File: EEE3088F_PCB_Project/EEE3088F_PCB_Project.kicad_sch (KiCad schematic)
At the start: 81 parts, among them IC1 DRV8833PWPR, IC2 DRV8833PWPR, IC3 TPS62067DSGR, IC5 INA219AIDCNR, IC7 TPS61088RHLR, J1 Conn_02x16_Odd_Even, J2 TYPE-C16PIN, J3 Conn_01x02, Q1 AO3400A, Q2 AO3400A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

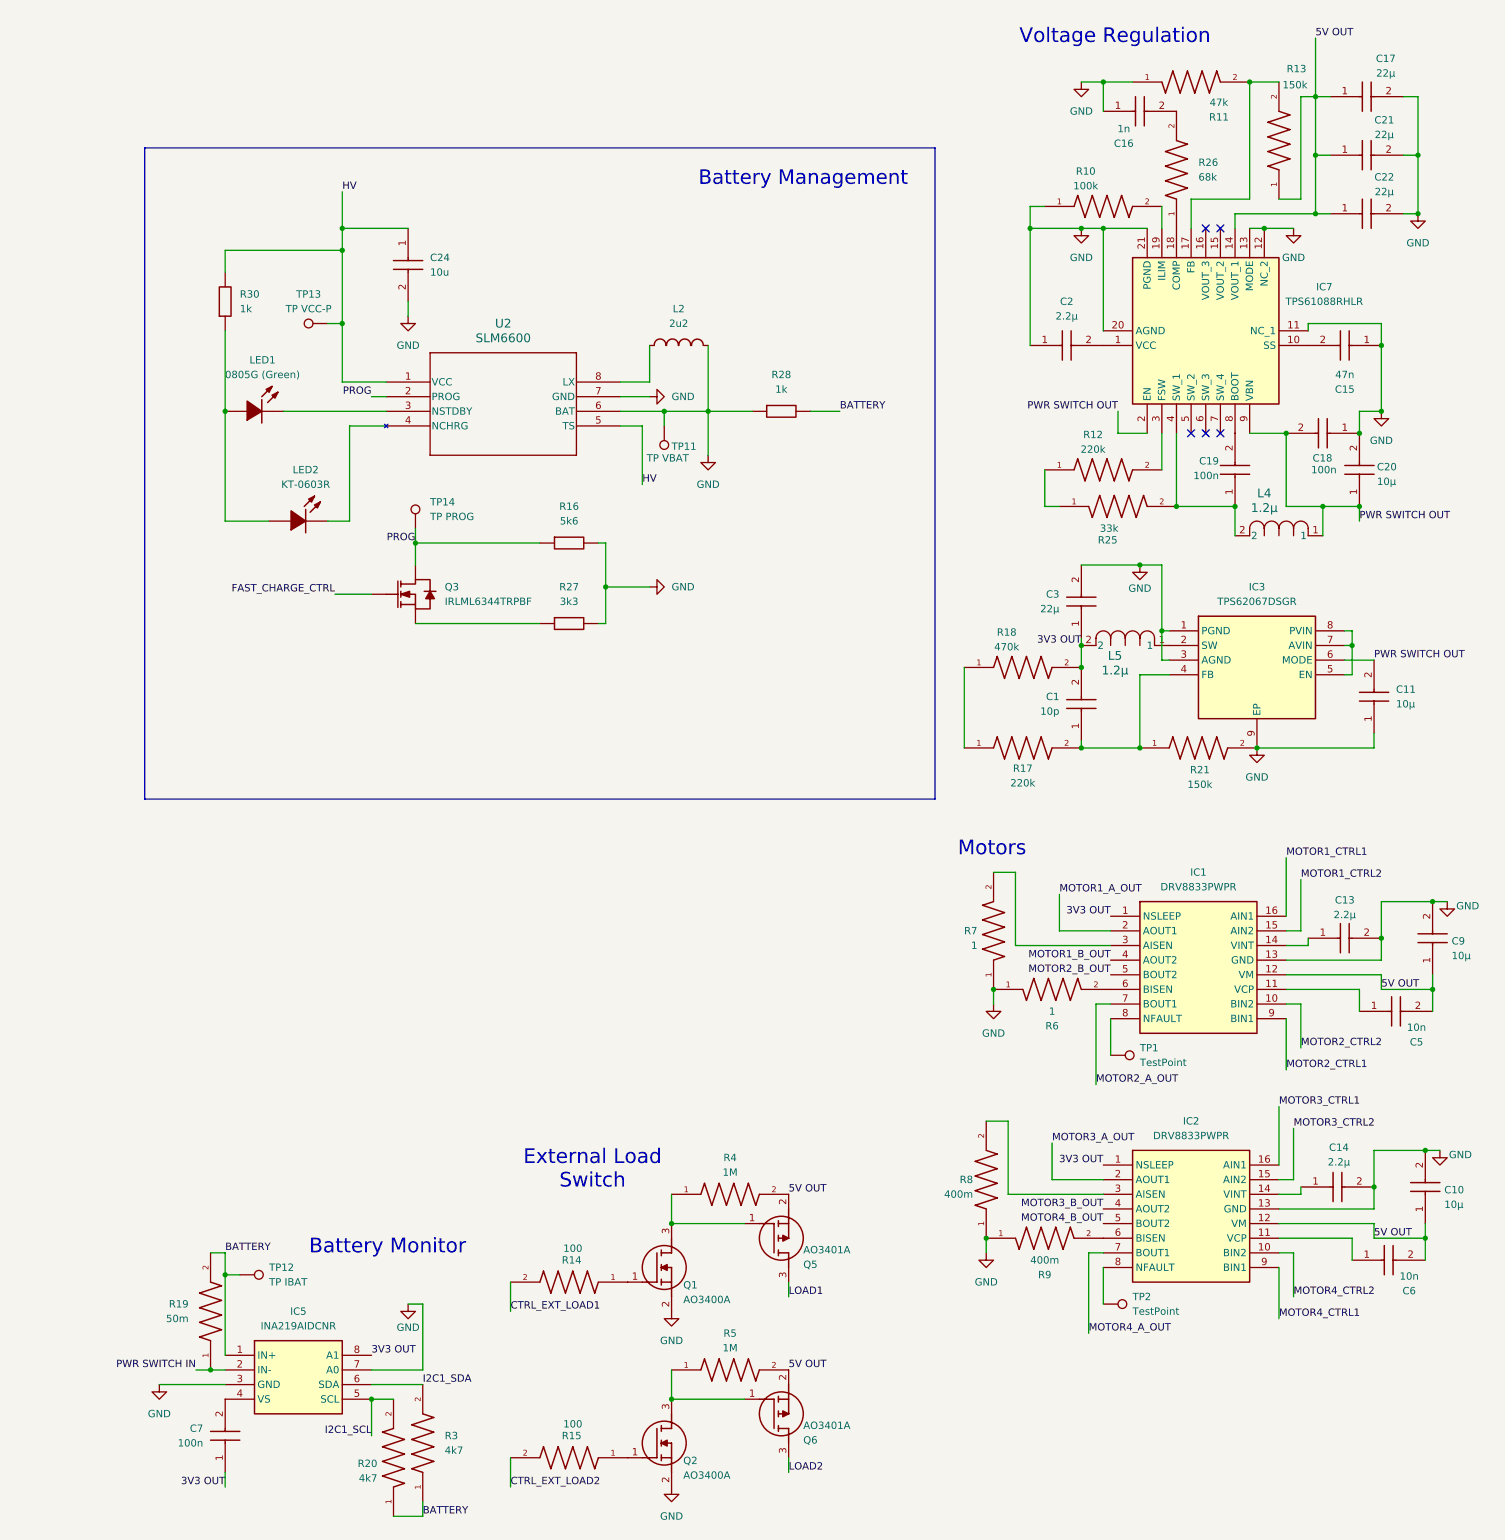
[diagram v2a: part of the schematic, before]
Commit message: V1.3.3
Added test points to my parts of the circuit
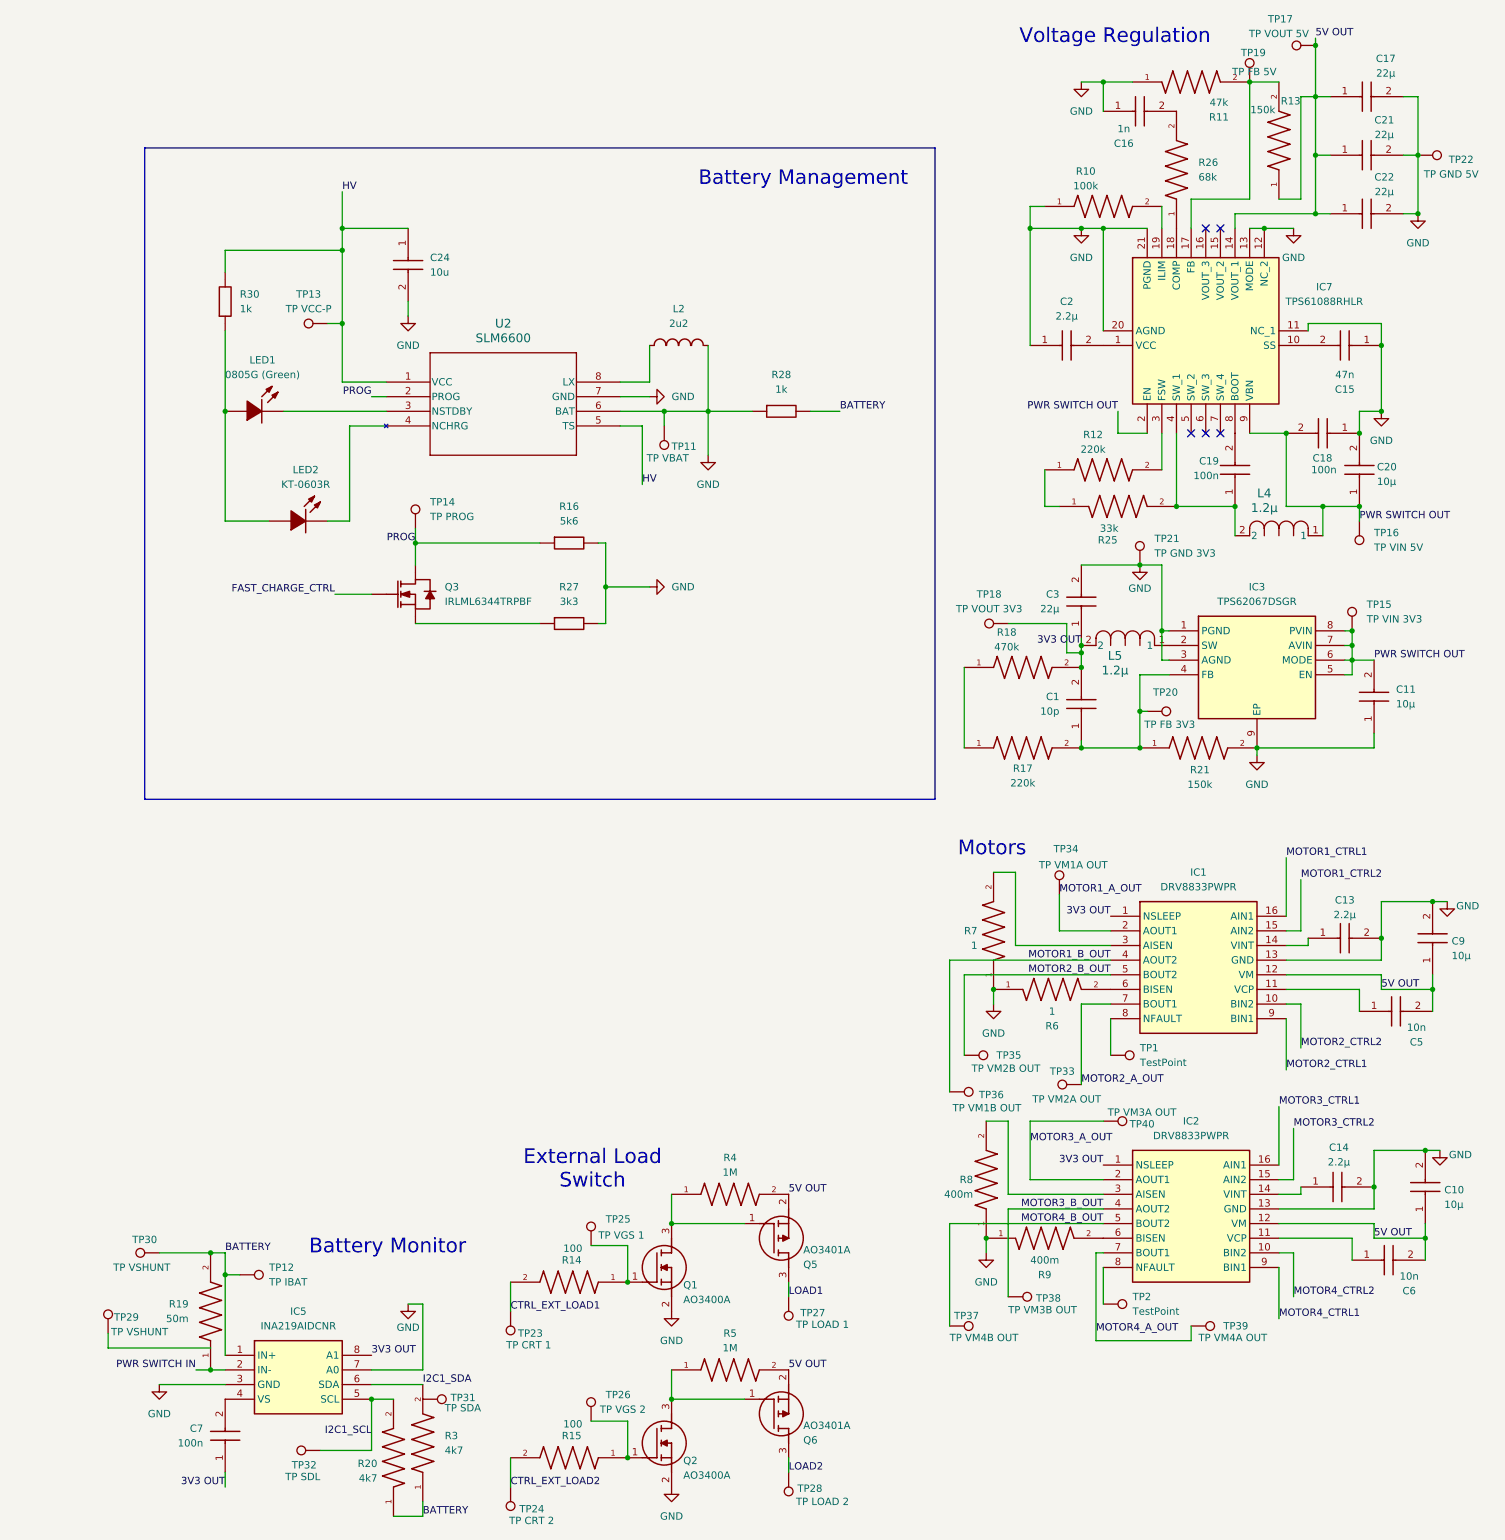
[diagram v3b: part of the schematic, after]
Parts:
- added TP15: TP VIN 3V3, symbol Connector:TestPoint
- added TP16: TP VIN 5V, symbol Connector:TestPoint
- added TP17: TP VOUT 5V, symbol Connector:TestPoint
- added TP18: TP VOUT 3V3, symbol Connector:TestPoint
- added TP19: TP FB 5V, symbol Connector:TestPoint
- added TP20: TP FB 3V3, symbol Connector:TestPoint
- added TP21: TP GND 3V3, symbol Connector:TestPoint
- added TP22: TP GND 5V, symbol Connector:TestPoint
- added TP23: TP CRT 1, symbol Connector:TestPoint
- added TP24: TP CRT 2, symbol Connector:TestPoint
- added TP25: TP VGS 1, symbol Connector:TestPoint
- added TP26: TP VGS 2, symbol Connector:TestPoint
- added TP27: TP LOAD 1, symbol Connector:TestPoint
- added TP28: TP LOAD 2, symbol Connector:TestPoint
- added TP29, TP30: TP VSHUNT, symbol Connector:TestPoint
- added TP31: TP SDA, symbol Connector:TestPoint
- added TP32: TP SDL, symbol Connector:TestPoint
- added TP33: TP VM2A OUT, symbol Connector:TestPoint
- added TP34: TP VM1A OUT, symbol Connector:TestPoint
- added TP35: TP VM2B OUT, symbol Connector:TestPoint
- added TP36: TP VM1B OUT, symbol Connector:TestPoint
- added TP37: TP VM4B OUT, symbol Connector:TestPoint
- added TP38: TP VM3B OUT, symbol Connector:TestPoint
- added TP39: TP VM4A OUT, symbol Connector:TestPoint
- added TP40: TP VM3A OUT, symbol Connector:TestPoint
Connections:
- net 3V3 OUT: now also TP18.1
- net 5V OUT: now also TP17.1
- net BATTERY: now also TP30.1
- net CTRL_EXT_LOAD1: now also TP23.1
- net CTRL_EXT_LOAD2: now also TP24.1
- net GND: now also TP21.1, TP22.1
- net I2C1_SCL: now also TP32.1
- net LOAD1: now also TP27.1
- net LOAD2: now also TP28.1
- net MOTOR1_A_OUT: now also TP34.1
- net MOTOR1_B_OUT: now also TP36.1
- net MOTOR2_A_OUT: now also TP33.1
- net MOTOR2_B_OUT: now also TP35.1
- net MOTOR3_A_OUT: now also TP40.1
- net MOTOR3_B_OUT: now also TP38.1
- net MOTOR4_A_OUT: now also TP39.1
- net MOTOR4_B_OUT: now also TP37.1
- net PWR SWITCH OUT: now also IC3.5 (EN), IC3.7 (AVIN), IC3.8 (PVIN), TP15.1, TP16.1
- net at Q2.1 (G), R15.1: now also TP26.1
- net at IC7.17 (FB), R11.2, R13.2: now also TP19.1
- net at C1.1, IC3.4 (FB), R17.2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: now also TP20.1
- net at Q1.1 (G), R14.1: now also TP25.1

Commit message: Revert "V1.3.3"
This reverts commit 82317ec0dd0d0933929f69b93ecb048d09c96738.
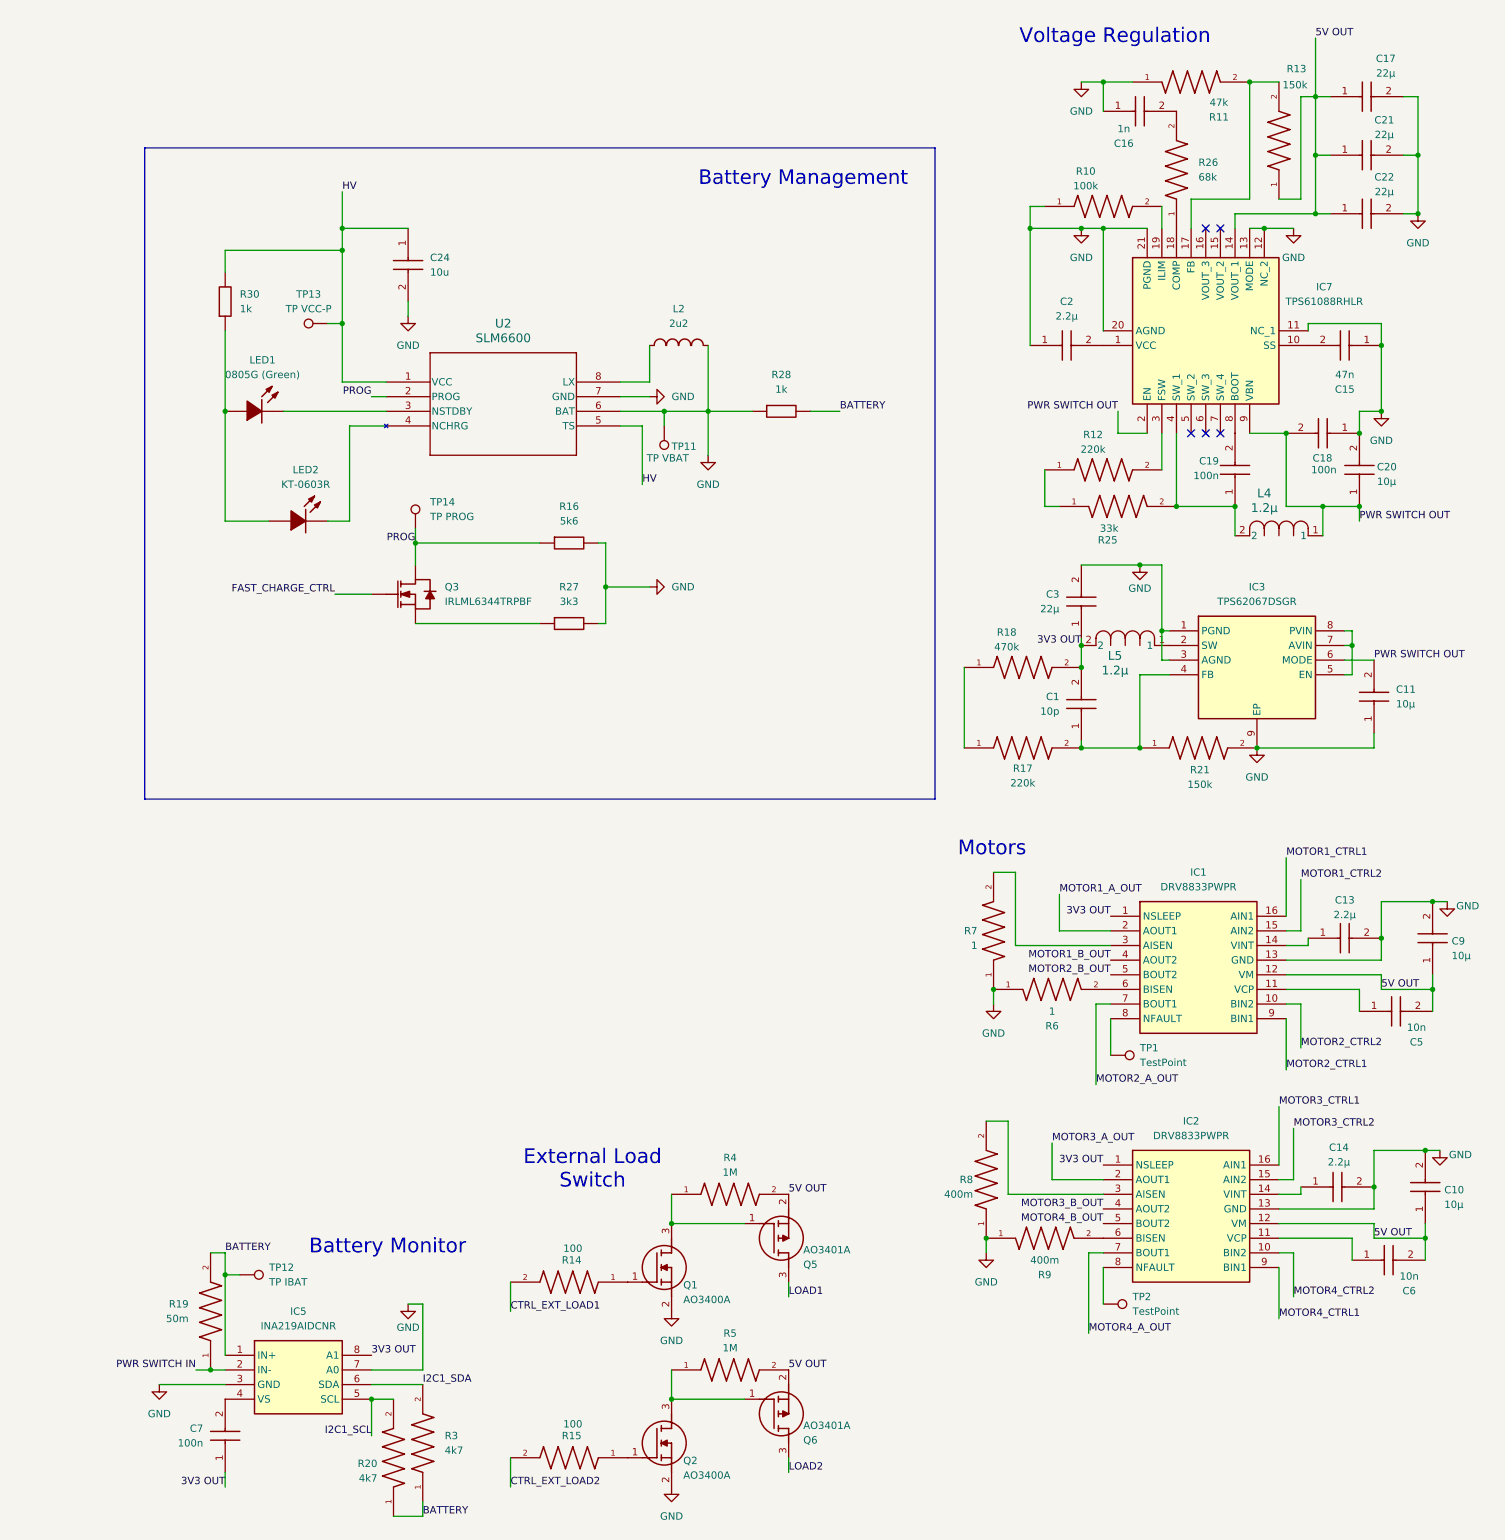
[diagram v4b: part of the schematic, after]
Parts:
- removed TP15: TP VIN 3V3, symbol Connector:TestPoint
- removed TP16: TP VIN 5V, symbol Connector:TestPoint
- removed TP17: TP VOUT 5V, symbol Connector:TestPoint
- removed TP18: TP VOUT 3V3, symbol Connector:TestPoint
- removed TP19: TP FB 5V, symbol Connector:TestPoint
- removed TP20: TP FB 3V3, symbol Connector:TestPoint
- removed TP21: TP GND 3V3, symbol Connector:TestPoint
- removed TP22: TP GND 5V, symbol Connector:TestPoint
- removed TP23: TP CRT 1, symbol Connector:TestPoint
- removed TP24: TP CRT 2, symbol Connector:TestPoint
- removed TP25: TP VGS 1, symbol Connector:TestPoint
- removed TP26: TP VGS 2, symbol Connector:TestPoint
- removed TP27: TP LOAD 1, symbol Connector:TestPoint
- removed TP28: TP LOAD 2, symbol Connector:TestPoint
- removed TP29, TP30: TP VSHUNT, symbol Connector:TestPoint
- removed TP31: TP SDA, symbol Connector:TestPoint
- removed TP32: TP SDL, symbol Connector:TestPoint
- removed TP33: TP VM2A OUT, symbol Connector:TestPoint
- removed TP34: TP VM1A OUT, symbol Connector:TestPoint
- removed TP35: TP VM2B OUT, symbol Connector:TestPoint
- removed TP36: TP VM1B OUT, symbol Connector:TestPoint
- removed TP37: TP VM4B OUT, symbol Connector:TestPoint
- removed TP38: TP VM3B OUT, symbol Connector:TestPoint
- removed TP39: TP VM4A OUT, symbol Connector:TestPoint
- removed TP40: TP VM3A OUT, symbol Connector:TestPoint
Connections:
- net PWR SWITCH OUT: no longer IC3.5 (EN), IC3.7 (AVIN), IC3.8 (PVIN)
- new net: IC3.5 (EN), IC3.7 (AVIN), IC3.8 (PVIN)
